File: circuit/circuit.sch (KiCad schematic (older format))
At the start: 2 parts

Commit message: Add more components to the schematic
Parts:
- added AFF?: CC56-12, symbol CC56-12
- added R? (x4): R, symbol R
- added SW?: Rotary_Encoder_Switch, symbol Rotary_Encoder_Switch
- added U? (x6): 74HC14, symbol 74HC14
- added U?: 74HC595, symbol 74HC595
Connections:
- wire segments 0 -> 8
- no-connect marks 0 -> 1
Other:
- moved on the sheet: IC?, P?
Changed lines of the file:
@@
 LIBS:contrib
 LIBS:valves
+LIBS:circuit-cache
 EELAYER 25 0
 EELAYER END
@@
 L ATMEGA328-P IC?
 U 1 1 5C36DC90
-P 4250 3600
-F 0 "IC?" H 3500 4850 50  0000 L BNN
-F 1 "ATMEGA328-P" H 4650 2200 50  0000 L BNN
-F 2 "DIL28" H 4250 3600 50  0000 C CIN
-F 3 "" H 4250 3600 50  0000 C CNN
-	1    4250 3600
-	1    0    0    -1
-$EndComp
-Text GLabel 5250 2800 2    60   Input ~ 0
+P 3150 2050
+F 0 "IC?" H 2400 3300 50  0000 L BNN
+F 1 "ATMEGA328-P" H 3550 650 50  0000 L BNN
+F 2 "DIL28" H 3150 2050 50  0000 C CIN
+F 3 "" H 3150 2050 50  0000 C CNN
+	1    3150 2050
+	1    0    0    -1
+$EndComp
+Text GLabel 4150 1250 2    60   Input ~ 0
 SPI_MOSI
-Text GLabel 5250 2700 2    60   Input ~ 0
+Text GLabel 4150 1150 2    60   Input ~ 0
 SPI_NSS
-Text GLabel 5250 3000 2    60   Input ~ 0
+Text GLabel 4150 1450 2    60   Input ~ 0
 SPI_SCK
-Text GLabel 5250 3100 2    60   Input ~ 0
+Text GLabel 4150 1550 2    60   Input ~ 0
 OSC1
-Text GLabel 5250 3200 2    60   Input ~ 0
+Text GLabel 4150 1650 2    60   Input ~ 0
 OSC2
-Text GLabel 5250 4700 2    60   Input ~ 0
+Text GLabel 4150 3150 2    60   Input ~ 0
 SOUND_OUT
 $Comp
 L CONN_02X03 P?
 U 1 1 5C36DD80
-P 6950 2550
-F 0 "P?" H 6950 2750 50  0000 C CNN
-F 1 "CONN_02X03" H 6950 2350 50  0000 C CNN
-F 2 "" H 6950 1350 50  0000 C CNN
-F 3 "" H 6950 1350 50  0000 C CNN
-	1    6950 2550
+P 5850 1000
+F 0 "P?" H 5850 1200 50  0000 C CNN
+F 1 "CONN_02X03" H 5850 800 50  0000 C CNN
+F 2 "" H 5850 -200 50  0000 C CNN
+F 3 "" H 5850 -200 50  0000 C CNN
+	1    5850 1000
 	-1   0    0    1
 $EndComp
@@
 L GND #PWR?
 U 1 1 5C36DEA9
-P 7200 2650
-F 0 "#PWR?" H 7200 2400 50  0001 C CNN
-F 1 "GND" H 7200 2500 50  0000 C CNN
-F 2 "" H 7200 2650 50  0000 C CNN
-F 3 "" H 7200 2650 50  0000 C CNN
-	1    7200 2650
-	1    0    0    -1
-$EndComp
-Text GLabel 7200 2550 2    60   Input ~ 0
+P 6100 1100
+F 0 "#PWR?" H 6100 850 50  0001 C CNN
+F 1 "GND" H 6100 950 50  0000 C CNN
+F 2 "" H 6100 1100 50  0000 C CNN
+F 3 "" H 6100 1100 50  0000 C CNN
+	1    6100 1100
+	1    0    0    -1
+$EndComp
+Text GLabel 6100 1000 2    60   Input ~ 0
 SPI_MOSI
-Text GLabel 5250 2900 2    60   Input ~ 0
+Text GLabel 4150 1350 2    60   Input ~ 0
 SPI_MISO
-Text GLabel 6700 2550 0    60   Input ~ 0
+Text GLabel 5600 1000 0    60   Input ~ 0
 SPI_SCK
-Text GLabel 6700 2450 0    60   Input ~ 0
+Text GLabel 5600 900  0    60   Input ~ 0
 SPI_MISO
-Text GLabel 5250 3950 2    60   Input ~ 0
+Text GLabel 4150 2400 2    60   Input ~ 0
 NRST
-Text GLabel 6700 2650 0    60   Input ~ 0
+Text GLabel 5600 1100 0    60   Input ~ 0
 NRST
+$Comp
+L 74HC14 U?
+U 1 1 5C36DFB5
+P 7050 1450
+F 0 "U?" H 7200 1550 50  0000 C CNN
+F 1 "74HC14" H 7250 1350 50  0000 C CNN
+F 2 "" H 7050 1450 50  0000 C CNN
+F 3 "" H 7050 1450 50  0000 C CNN
+	1    7050 1450
+	1    0    0    -1
+$EndComp
+$Comp
+L 74HC14 U?
+U 2 1 5C36DFEC
+P 7050 1750
+F 0 "U?" H 7200 1850 50  0000 C CNN
+F 1 "74HC14" H 7250 1650 50  0000 C CNN
+F 2 "" H 7050 1750 50  0000 C CNN
+F 3 "" H 7050 1750 50  0000 C CNN
+	2    7050 1750
+	1    0    0    -1
+$EndComp
+$Comp
+L 74HC14 U?
+U 3 1 5C36E019
+P 7050 2050
+F 0 "U?" H 7200 2150 50  0000 C CNN
+F 1 "74HC14" H 7250 1950 50  0000 C CNN
+F 2 "" H 7050 2050 50  0000 C CNN
+F 3 "" H 7050 2050 50  0000 C CNN
+	3    7050 2050
+	1    0    0    -1
+$EndComp
+$Comp
+L 74HC14 U?
+U 4 1 5C36E056
+P 7050 2350
+F 0 "U?" H 7200 2450 50  0000 C CNN
+F 1 "74HC14" H 7250 2250 50  0000 C CNN
+F 2 "" H 7050 2350 50  0000 C CNN
+F 3 "" H 7050 2350 50  0000 C CNN
+	4    7050 2350
+	1    0    0    -1
+$EndComp
+$Comp
+L 74HC14 U?
+U 5 1 5C36E0A3
+P 7050 2650
+F 0 "U?" H 7200 2750 50  0000 C CNN
+F 1 "74HC14" H 7250 2550 50  0000 C CNN
+F 2 "" H 7050 2650 50  0000 C CNN
+F 3 "" H 7050 2650 50  0000 C CNN
+	5    7050 2650
+	1    0    0    -1
+$EndComp
+$Comp
+L 74HC14 U?
+U 6 1 5C36E0E6
+P 7050 2950
+F 0 "U?" H 7200 3050 50  0000 C CNN
+F 1 "74HC14" H 7250 2850 50  0000 C CNN
+F 2 "" H 7050 2950 50  0000 C CNN
+F 3 "" H 7050 2950 50  0000 C CNN
+	6    7050 2950
+	1    0    0    -1
+$EndComp
+$Comp
+L 74HC595 U?
+U 1 1 5C36E119
+P 2800 4800
+F 0 "U?" H 2950 5400 50  0000 C CNN
+F 1 "74HC595" H 2800 4200 50  0000 C CNN
+F 2 "" H 2800 4800 50  0000 C CNN
+F 3 "" H 2800 4800 50  0000 C CNN
+	1    2800 4800
+	1    0    0    -1
+$EndComp
+Text GLabel 2100 4550 0    60   Input ~ 0
+SPI_SCK
+Text GLabel 2100 4650 0    60   Input ~ 0
+SPI_NSS
+Text GLabel 2100 4350 0    60   Input ~ 0
+SPI_MOSI
+$Comp
+L GND #PWR?
+U 1 1 5C36EC35
+P 2100 4950
+F 0 "#PWR?" H 2100 4700 50  0001 C CNN
+F 1 "GND" H 2100 4800 50  0000 C CNN
+F 2 "" H 2100 4950 50  0000 C CNN
+F 3 "" H 2100 4950 50  0000 C CNN
+	1    2100 4950
+	1    0    0    -1
+$EndComp
+$Comp
+L Rotary_Encoder_Switch SW?
+U 1 1 5C36ECAC
+P 5800 1600
+F 0 "SW?" H 5800 1860 50  0000 C CNN
+F 1 "Rotary_Encoder_Switch" H 5800 1340 50  0000 C CNN
+F 2 "" H 5700 1760 50  0001 C CNN
+F 3 "" H 5800 1860 50  0001 C CNN
+	1    5800 1600
+	1    0    0    -1
+$EndComp
+$Comp
+L CC56-12 AFF?
+U 1 1 5C36EE87
+P 4750 4650
+F 0 "AFF?" H 4750 5400 50  0000 C CNN
+F 1 "CC56-12" H 4750 5300 50  0000 C CNN
+F 2 "" H 4250 4650 50  0000 C CNN
+F 3 "" H 4250 4650 50  0000 C CNN
+	1    4750 4650
+	0    1    1    0
+$EndComp
+NoConn ~ 3500 5250
+Wire Wire Line
+	3500 4350 4050 4350
+Wire Wire Line
+	3500 4450 4050 4450
+Wire Wire Line
+	3500 4550 4050 4550
+Wire Wire Line
+	3500 4650 4050 4650
+Wire Wire Line
+	3500 4750 4050 4750
+Wire Wire Line
+	3500 4850 4050 4850
+Wire Wire Line
+	3500 4950 4050 4950
+Wire Wire Line
+	3500 5050 4050 5050
+$Comp
+L R R?
+U 1 1 5C36F513
+P 5600 3950
+F 0 "R?" V 5680 3950 50  0000 C CNN
+F 1 "R" V 5600 3950 50  0000 C CNN
+F 2 "" V 5530 3950 50  0000 C CNN
+F 3 "" H 5600 3950 50  0000 C CNN
+	1    5600 3950
+	0    1    1    0
+$EndComp
+$Comp
+L R R?
+U 1 1 5C36F6A3
+P 5600 4450
+F 0 "R?" V 5680 4450 50  0000 C CNN
+F 1 "R" V 5600 4450 50  0000 C CNN
+F 2 "" V 5530 4450 50  0000 C CNN
+F 3 "" H 5600 4450 50  0000 C CNN
+	1    5600 4450
+	0    1    1    0
+$EndComp
+$Comp
+L R R?
+U 1 1 5C36F708
+P 5600 4950
+F 0 "R?" V 5680 4950 50  0000 C CNN
+F 1 "R" V 5600 4950 50  0000 C CNN
+F 2 "" V 5530 4950 50  0000 C CNN
+F 3 "" H 5600 4950 50  0000 C CNN
+	1    5600 4950
+	0    1    1    0
+$EndComp
+$Comp
+L R R?
+U 1 1 5C36F756
+P 5600 5450
+F 0 "R?" V 5680 5450 50  0000 C CNN
+F 1 "R" V 5600 5450 50  0000 C CNN
+F 2 "" V 5530 5450 50  0000 C CNN
+F 3 "" H 5600 5450 50  0000 C CNN
+	1    5600 5450
+	0    1    1    0
+$EndComp
 $EndSCHEMATC

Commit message: Add more schematics, music notes and menus
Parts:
- removed AFF?: CC56-12, symbol CC56-12
- removed IC?: ATMEGA328-P, DIL28, symbol ATMEGA328-P
- removed P?: CONN_02X03, symbol CONN_02X03
- removed R? (x4): R, symbol R
- removed U? (x6): 74HC14, symbol 74HC14
- removed U?: 74HC595, symbol 74HC595
- added C? (x5): 0.1u, symbol Device:C
- added C?: 47u, symbol Device:CP1
- added D? (x3): LED, symbol Device:LED
- added J?: Conn_02x03_Odd_Even, symbol Connector_Generic:Conn_02x03_Odd_Even
- added J?: Conn_01x02_Male, symbol Connector:Conn_01x02_Male
- added R? (x10): 10k, symbol Device:R
- added R?: 1k, symbol Device:R
- added R? (x3): 510, symbol Device:R
- added R? (x4): 330, symbol Device:R
- added SW? (x2): SW_Push, symbol Switch:SW_Push
- added SW?: SW_SPDT, symbol Switch:SW_SPDT
- added U?: ATmega328P-PU, Package_DIP:DIP-28_W7.62mm, symbol MCU_Microchip_ATmega:ATmega328P-PU
- added U?: CC56-12SRWA, Display_7Segment:CA56-12SRWA, symbol Display_Character:CC56-12SRWA
- added U? (x7): 74HC14, symbol 74xx:74HC14
- added U?: 74HC595, symbol 74xx:74HC595
- SW?: symbol Rotary_Encoder_Switch -> Device:Rotary_Encoder_Switch
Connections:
- net labels added: +5C, +5V, BUTTON0, BUTTON1, DIG0, DIG1, DIG2, DIG3, DIGSEL0, DIGSEL1, DIGSEL2, DIGSEL3, ENC_A, ENC_B, ENC_BUTTON, FREE_PIN, LED0, LED1, LED2, SWITCH0
- wire segments 8 -> 81
- no-connect marks 1 -> 3

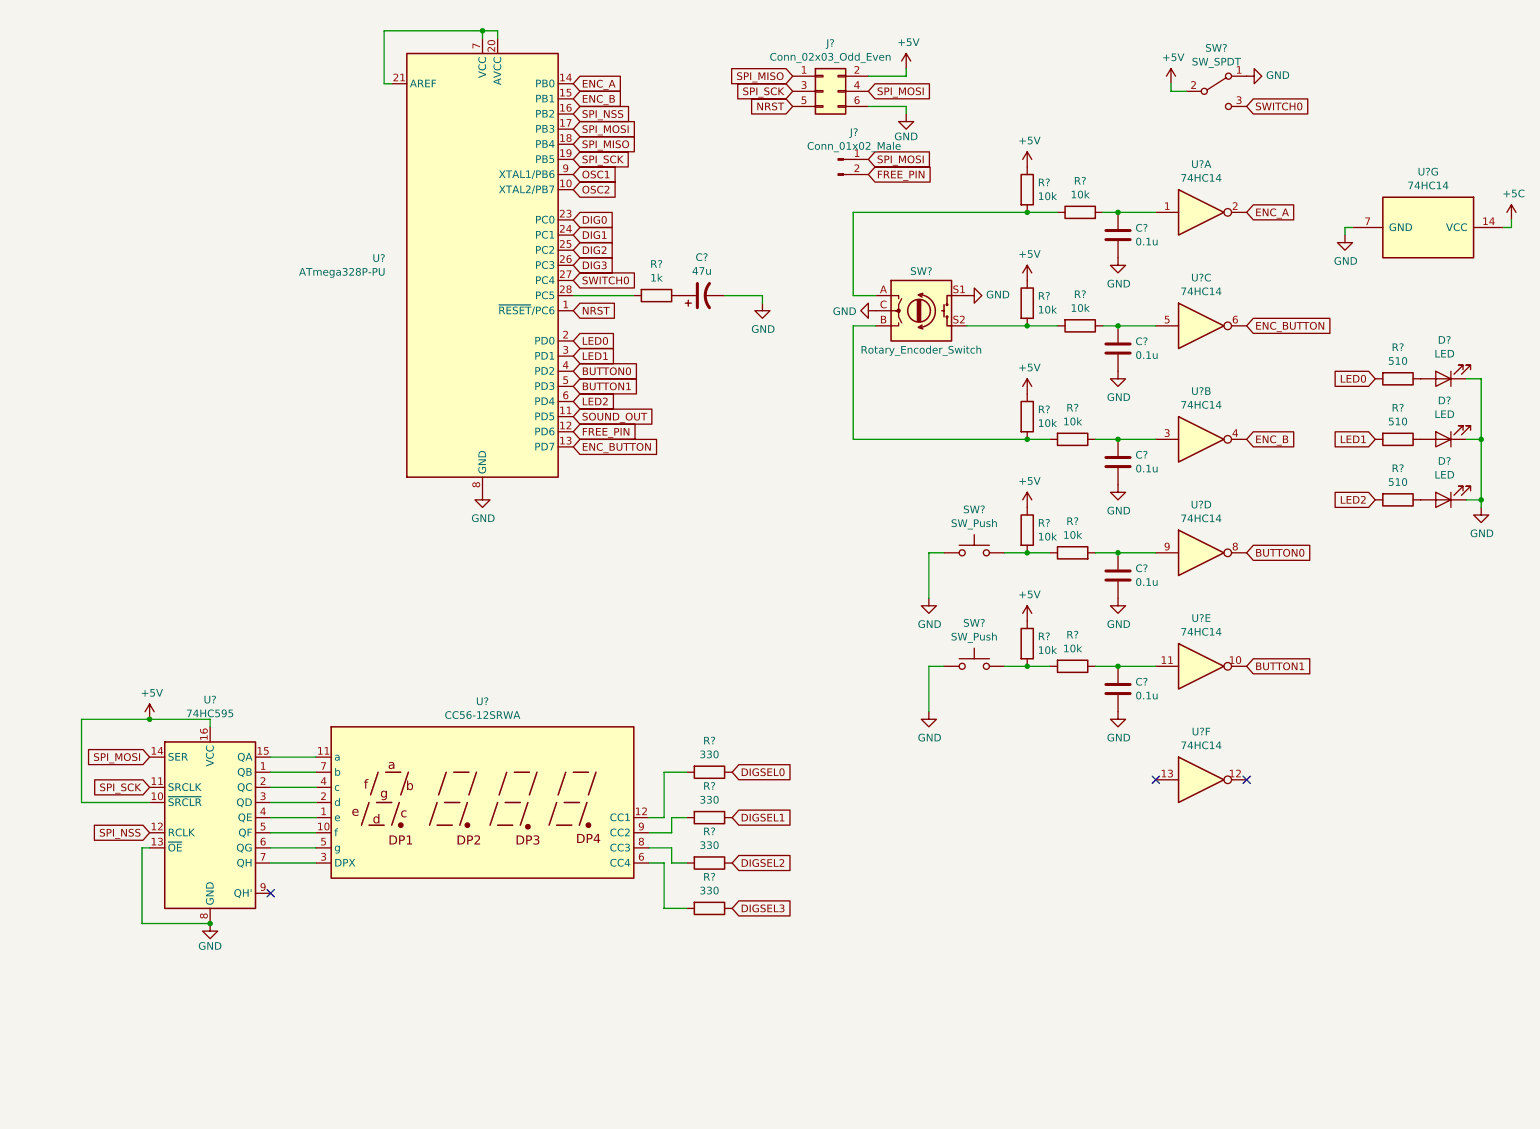
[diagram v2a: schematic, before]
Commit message: Migrate to bare atmega328p
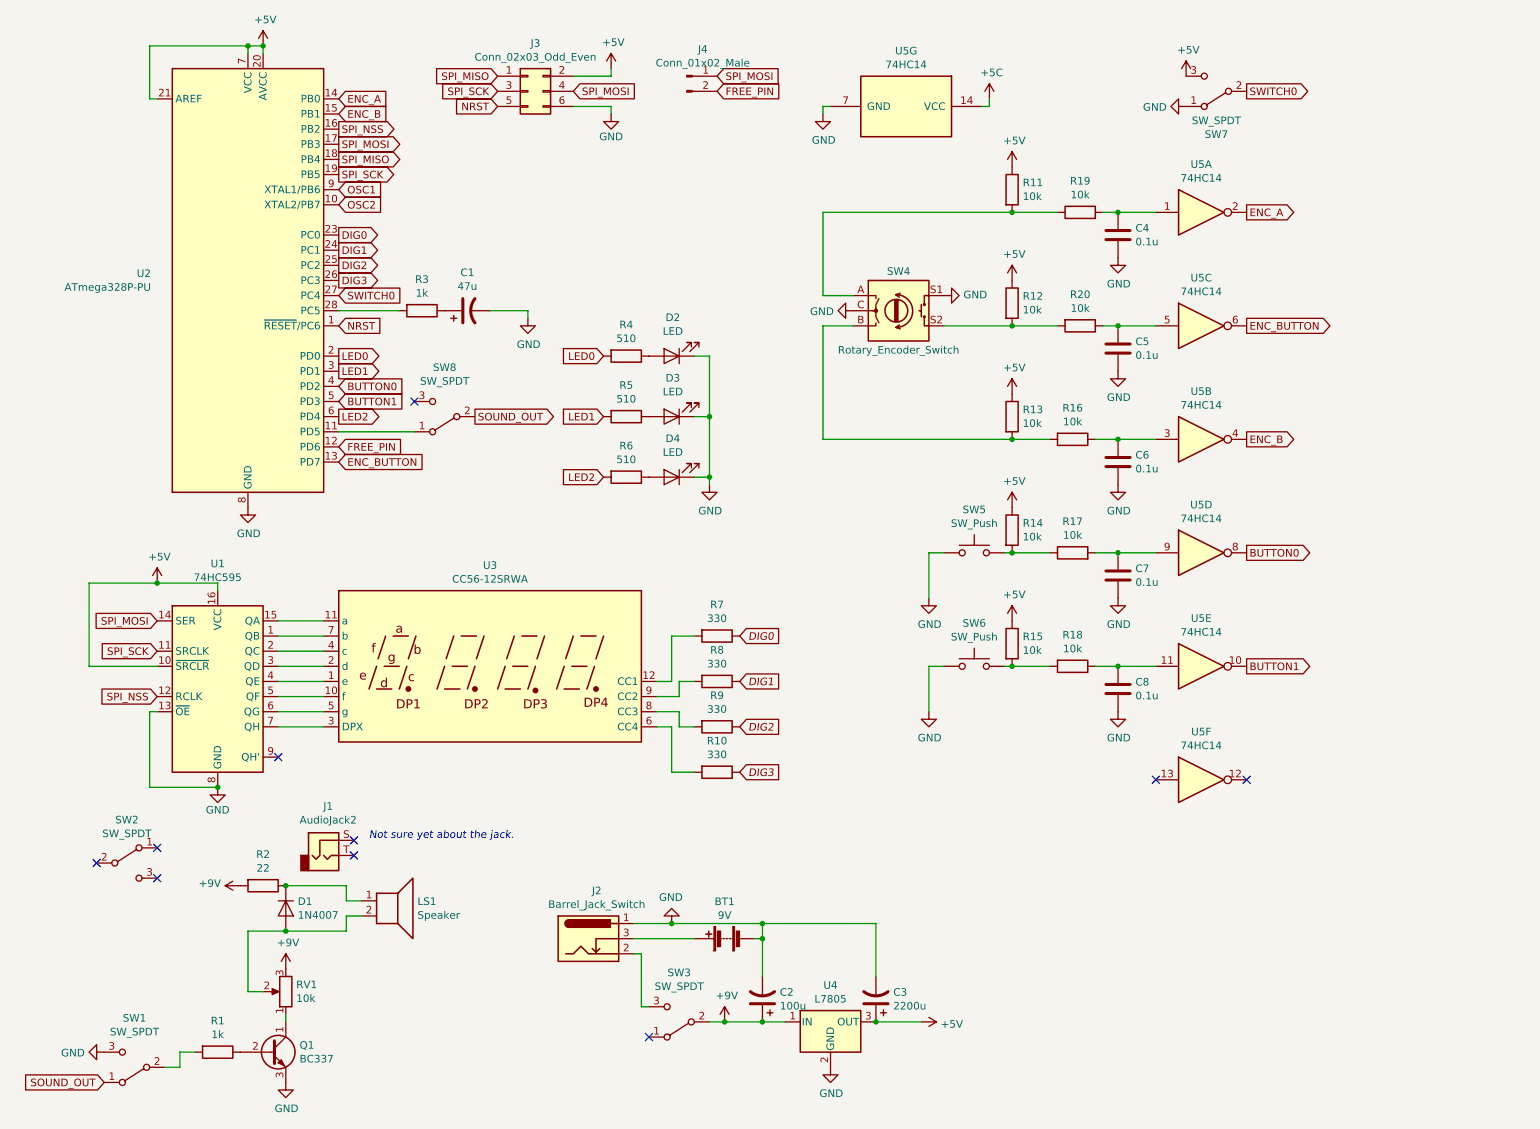
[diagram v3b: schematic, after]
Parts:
- added BT1: 9V, symbol Device:Battery
- added C2: 100u, symbol Device:CP1
- added C3: 2200u, symbol Device:CP1
- added D1: 1N4007, Diode_THT:D_DO-41_SOD81_P10.16mm_Horizontal, symbol Diode:1N4007
- added J1: AudioJack2, symbol Connector:AudioJack2
- added J2: Barrel_Jack_Switch, symbol Connector:Barrel_Jack_Switch
- added LS1: Speaker, symbol Device:Speaker
- added Q1: BC337, Package_TO_SOT_THT:TO-92_Inline, symbol Transistor_BJT:BC337
- added R1: 1k, symbol Device:R
- added R2: 22, symbol Device:R
- added RV1: 10k, symbol Device:R_POT
- added SW1, SW2, SW3, SW8: SW_SPDT, symbol Switch:SW_SPDT
- added U4: L7805, symbol Regulator_Linear:L7805
- gave numbers to parts that had none: 37
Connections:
- net DIGSEL0 is gone; now on net DIG0: R7.1
- net DIGSEL1 is gone; now on net DIG1: R8.1
- net DIGSEL2 is gone; now on net DIG2: R9.1
- net DIGSEL3 is gone; now on net DIG3: R10.1
- net +5V: now also SW7.3 (C), U2.20 (AVCC), U2.21 (AREF), U2.7 (VCC), C3.1, U4.3 (OUT); no longer SW7.2 (B)
- net GND: now also BT1.2 (-), C2.2, C3.2, J2.1, Q1.3 (E), SW1.3 (C), U4.2 (GND)
- net SOUND_OUT: now also SW1.1 (A), SW8.2 (B); no longer U2.11 (PD5)
- net SWITCH0: now also SW7.2 (B); no longer SW7.3 (C)
- new net: SW8.1 (A), U2.11 (PD5)
- new net: Q1.1 (C), RV1.1
- new net: Q1.2 (B), R1.1
- new net: R1.2, SW1.2 (B)
- new net: D1.2 (A), LS1.2, RV1.2
- new net: D1.1 (K), LS1.1, R2.1
- new net: J2.2, SW3.3 (C)
- new net: BT1.1 (+), J2.3
- new net +9V: C2.1, R2.2, RV1.3, SW3.2 (B), U4.1 (IN)
- no-connect marks 3 -> 10
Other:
- note added: "Not sure yet about the jack."
- moved on the sheet: C1, D2, D3, D4, J3, J4, R10, R11, R12, R13, R14, R15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

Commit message: Update schematic
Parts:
- removed J4: Conn_01x02_Male, symbol Connector:Conn_01x02_Male
- added C11: 0.1u, symbol Device:C
- added C2, C3: 22p, symbol Device:C
- added R16, R20: 10k, symbol Device:R
- added SW8: SW_Push, symbol Switch:SW_Push
- added Y1: 16M, symbol Device:Crystal
- renumbered C8 to C10, C2 to C4, C3 to C5, C4 to C6, C5 to C7, C6 to C8, C7 to C9, R16 to R17, R17 to R18, R18 to R19, R19 to R21, R20 to R22, SW2 to SW1, SW1 to SW2, SW8 to SW3, SW3 to SW4, SW4 to SW5, SW5 to SW6, SW6 to SW7, SW7 to SW9
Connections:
- net labels added: BUTTON2
- net labels removed: +5C, FREE_PIN, OSC1, OSC2
- wire segments 108 -> 129
- no-connect marks 10 -> 7
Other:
- moved on the sheet: D2, D3, D4, J3, R4, R5, R6, SW3
